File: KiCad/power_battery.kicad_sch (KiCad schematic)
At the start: 47 parts, among them IC1 BQ26221PW, J4 Conn_01x03_BATT, Q2 AO3400A, Q3 AO3400A, U2 DW01A, U3 TXB0101DBV, U4 BQ51050BRHL, U5 PAM2306AYPKE

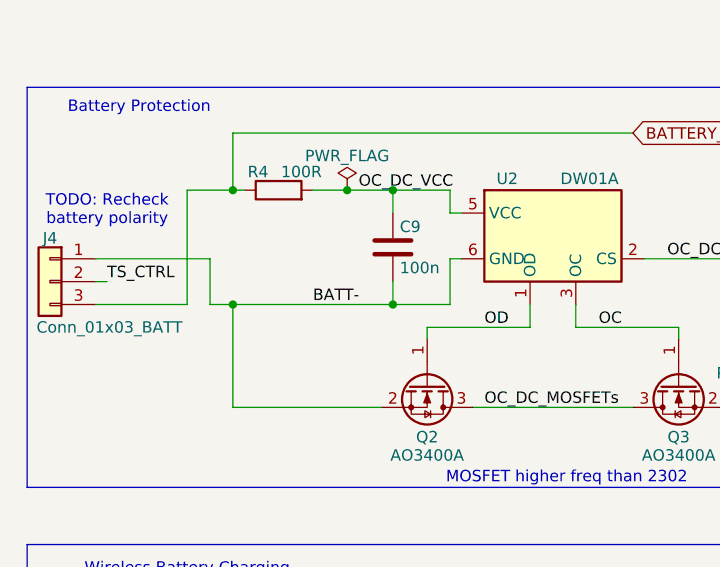
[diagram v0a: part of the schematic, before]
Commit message: Add Power Flag on GND
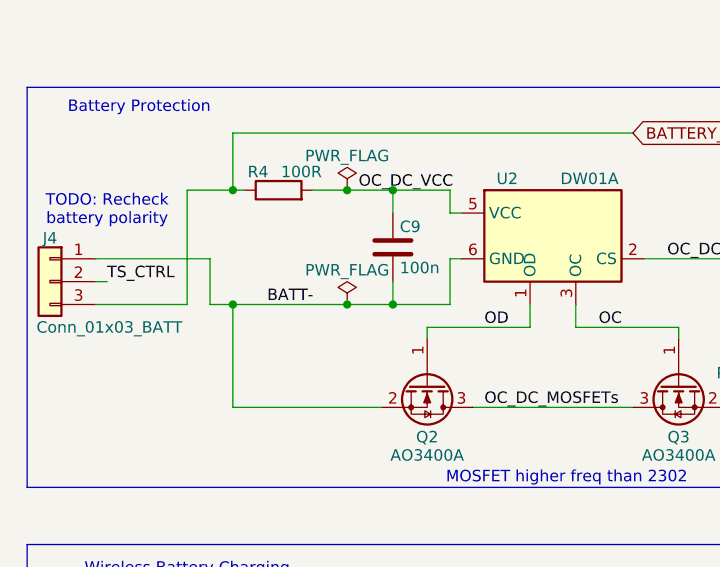
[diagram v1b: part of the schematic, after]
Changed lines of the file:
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@@
 	)
 	(junction
+		(at 54.61 52.07)
+		(diameter 0)
+		(color 0 0 0 0)
+	)
+	(junction
 		(at 41.91 52.07)
 		(diameter 0)
@@
 	(wire
 		(pts
-			(xy 41.91 52.07) (xy 59.69 52.07)
+			(xy 41.91 52.07) (xy 54.61 52.07)
 		)
 		(stroke
@@
 	(wire
 		(pts
+			(xy 54.61 52.07) (xy 59.69 52.07)
+		)
+		(stroke
+			(width 0)
+			(type default)
+		)
+	)
+	(wire
+		(pts
 			(xy 104.14 166.37) (xy 104.14 168.91)
 		)
@@
 	)
 	(label "BATT-"
-		(at 50.8 52.07 0)
+		(at 45.72 52.07 0)
 		(effects
 			(font
@@
 					(unit 1)
 				)
+			)
+		)
+	)
+	(symbol
+		(lib_id "power:PWR_FLAG")
+		(at 54.61 52.07 0)
+		(unit 1)
+		(exclude_from_sim no)
+		(in_bom yes)
+		(on_board yes)
+		(dnp no)
+		(property "Reference" "#FLG06"
+			(at 54.61 50.165 0)
+			(effects
+				(font
+					(size 1.27 1.27)
+				)
+				(hide yes)
+			)
+		)
+		(property "Value" "PWR_FLAG"
+			(at 54.61 48.26 0)
+			(effects
+				(font
+					(size 1.27 1.27)
+				)
+			)
+		)
+		(property "Footprint" ""
+			(at 54.61 52.07 0)
+			(effects
+				(font
+					(size 1.27 1.27)
+				)
+				(hide yes)
+			)
+		)
+		(property "Datasheet" "~"
+			(at 54.61 52.07 0)
+			(effects
+				(font
+					(size 1.27 1.27)
+				)
+				(hide yes)
+			)
+		)
+		(property "Description" "Special symbol for telling ERC where power comes from"
+			(at 54.61 52.07 0)
+			(effects
+				(font
+					(size 1.27 1.27)
+				)
+				(hide yes)
+			)
+		)
+		(pin "1"
+		)
+		(instances
+			(project "STDC"
+				(path "/643c756f-a801-466b-9148-7370ee6a5e00/6fbfac7b-b6a0-440e-84eb-56b1f74b7943"
+					(reference "#FLG06")
+					(unit 1)
+				)

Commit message: Create Revision 0.0.1
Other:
- company: (none) -> ETH Zurich: Center for Project Based Learning
- title: (none) -> STDC: Power & Battery
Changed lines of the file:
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@@
 	(generator_version "9.0")
 	(paper "A4")
+	(title_block
+		(title "STDC: Power & Battery")
+		(date "2026-03-05")
+		(rev "0.0.1")
+		(company "ETH Zurich: Center for Project Based Learning")
+	)
 	(rectangle
 		(start 19.05 78.74)

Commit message: Add TODO to discuss tomorrow
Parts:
- R11: value 1k -> 680R
- R15: value 200R -> 220R
- R16: value 2.4k -> 2k2
- R4: value 100R -> 150R
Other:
- note added: "R_{FOD} = 220R => R_ILIM=150R => 370R close to 375R target I_{BULk}=K_{ILIM} / R_{ILIM} = 300 / 370 = 811mA = 0.8A"
- note added: "R_{TERM}: Original 2k4, with 2k2: 9.17% Term Current with 2k4: 10% Term Current"
- note added: "TODO: Where should this (FGND) tie to?"
- note removed: "I_{BULk}=800mA R_{ILIM}=393R/(0.8A)=393R R_{FOD} = 220R => R_ILIM=173R"
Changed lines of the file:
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@@
 		)
 	)
-	(text "I_{BULk}=800mA\nR_{ILIM}=393R/(0.8A)=393R\nR_{FOD} = 220R => R_ILIM=173R"
+	(text "R_{FOD} = 220R => R_ILIM=150R => 370R\nclose to 375R target\nI_{BULk}=K_{ILIM} / R_{ILIM} = 300 / 370 = 811mA = 0.8A"
 		(exclude_from_sim no)
-		(at 159.004 145.034 0)
+		(at 142.494 136.144 0)
 		(effects
 			(font
@@
 		)
 	)
+	(text "TODO: Where should this \n(FGND) tie to?"
+		(exclude_from_sim no)
+		(at 266.7 66.548 0)
+		(effects
+			(font
+				(size 1.27 1.27)
+			)
+		)
+	)
 	(text "Wireless Charging RX Coil"
 		(exclude_from_sim no)
@@
 		)
 	)
+	(text "R_{TERM}: Original 2k4, \nwith 2k2: 9.17% Term Current\nwith 2k4: 10% Term Current"
+		(exclude_from_sim no)
+		(at 192.278 144.526 0)
+		(effects
+			(font
+				(size 1.27 1.27)
+			)
+		)
+	)
 	(text "TODO: Recheck \nbattery polarity"
 		(exclude_from_sim no)
@@
 		(dnp no)
 		(property "Reference" "R11"
-			(at 183.642 92.456 90)
+			(at 182.372 92.456 90)
 			(effects
 				(font
@@
 			)
 		)
-		(property "Value" "1k"
-			(at 187.96 92.456 90)
+		(property "Value" "680R"
+			(at 188.468 92.456 90)
 			(effects
 				(font
@@
 			)
 		)
-		(property "Value" "100R"
+		(property "Value" "150R"
 			(at 49.53 37.338 90)
 			(effects
@@
 			)
 		)
-		(property "Value" "200R"
+		(property "Value" "220R"
 			(at 170.18 137.16 0)
 			(effects
@@
 			)
 		)
-		(property "Value" "2.4k"
+		(property "Value" "2k2"
 			(at 179.07 137.16 0)
 			(effects

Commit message: Added some TODOs, fixed some TODOs
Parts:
- added C15: 100n, symbol Device:C
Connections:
- net BAT_STAT_C_COUNT is gone; now on net GND: R10.2, R8.2
- net +1V8: now also C15.1
- net +3.3V: no longer R17.2
- net BATT-: now also C10.2, C11.2, C12.2, C13.2, IC1.3 (VSS), R10.1, R6.2, R7.2, U3.2 (GND), C15.2
- net GND: no longer C10.2, C11.2, C12.2, C13.2, IC1.3 (VSS), R10.1, R6.2, R7.2, U3.2 (GND)
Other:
- note added: "TODO: Saturation Current at Peak Current * DCDc With Display ON?"
- note removed: "TODO: Where should this (FGND) tie to?"
- moved on the sheet: C10, C11, C12, C13, IC1, R10, R6, R7, R9, U3

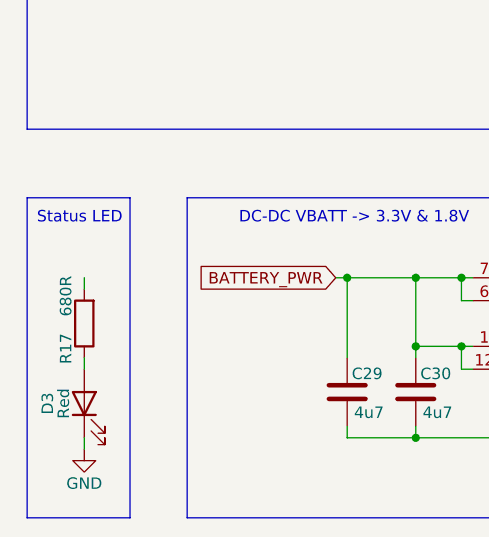
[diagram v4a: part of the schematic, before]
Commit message: Fix JTAG connector
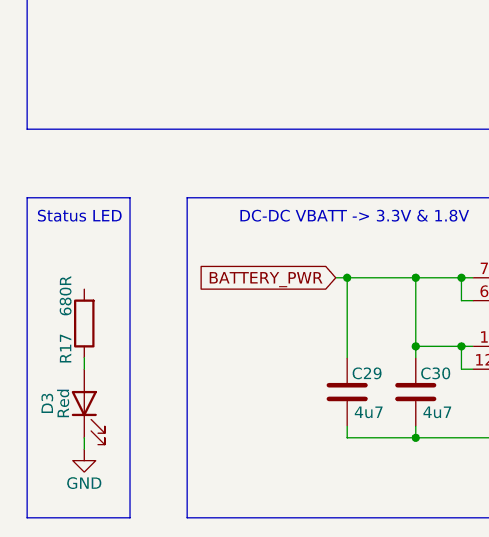
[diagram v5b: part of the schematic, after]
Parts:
- C15: footprint (none) -> Capacitor_SMD:C_0402_1005Metric
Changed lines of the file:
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@@
-	(wire
-		(pts
-			(xy 25.4 166.37) (xy 25.4 167.64)
-		)
-		(stroke
-			(width 0)
-			(type default)
-		)
-	)
 	(wire
 		(pts
@@
 			)
 		)
-		(property "Footprint" ""
+		(property "Footprint" "Capacitor_SMD:C_0402_1005Metric"
 			(at 141.9352 62.23 0)
 			(effects

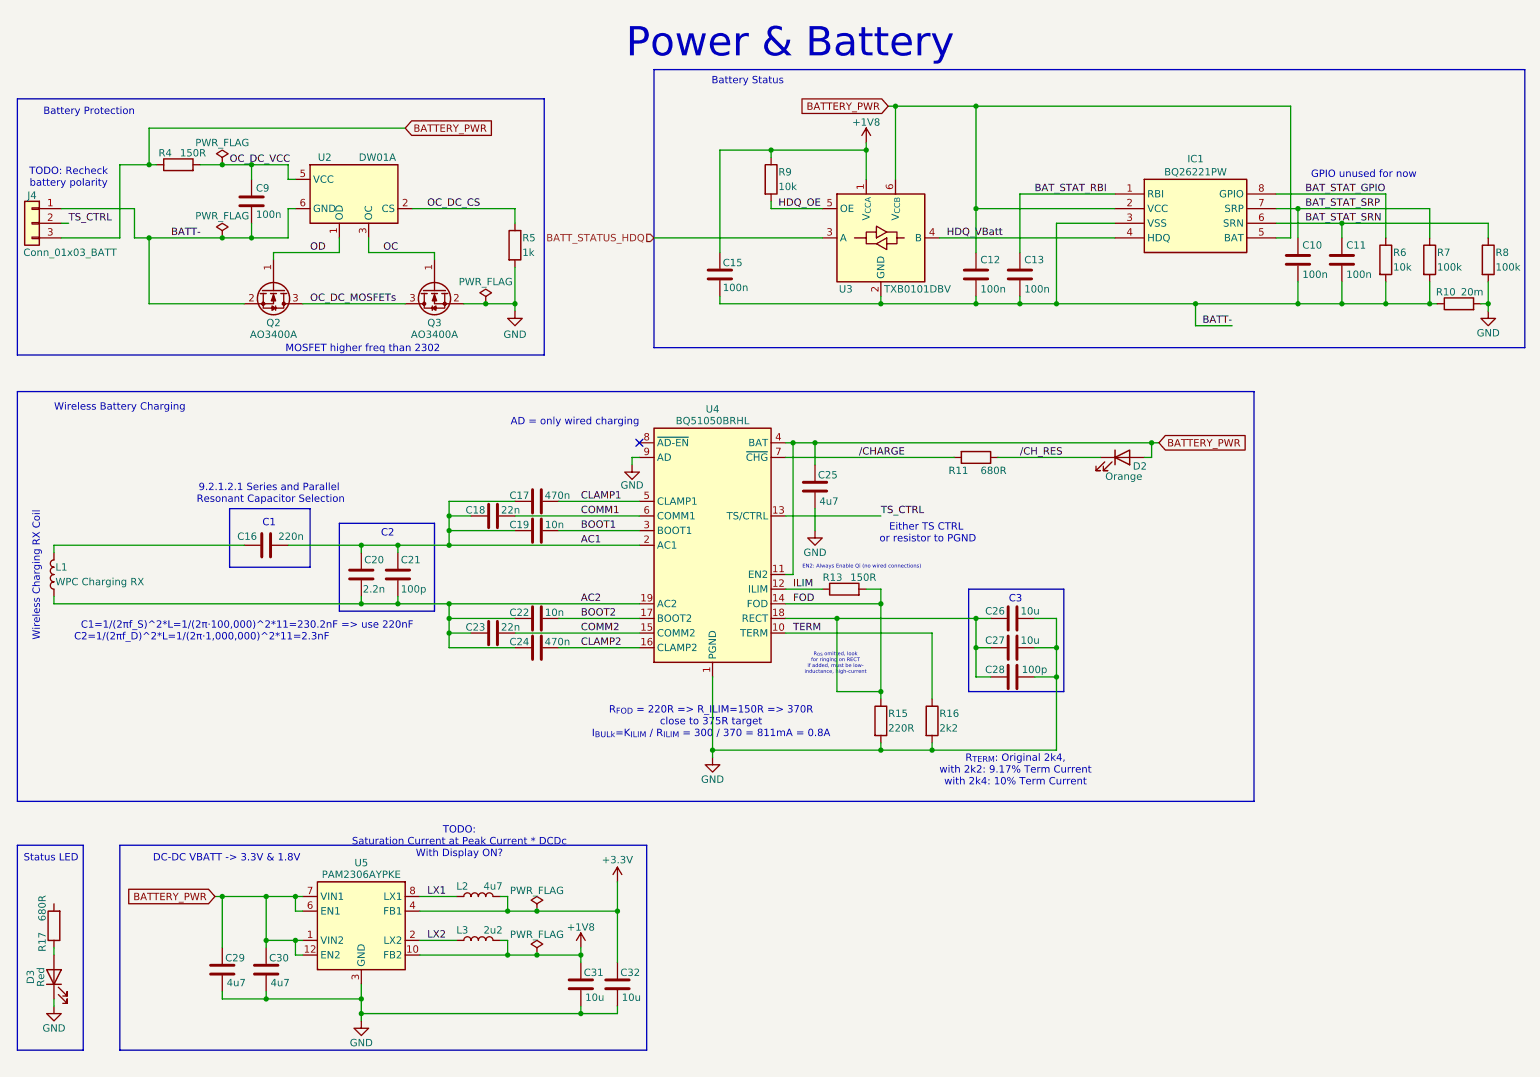
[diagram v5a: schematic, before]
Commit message: Testing connectors, SPI2 pinout, reannotate
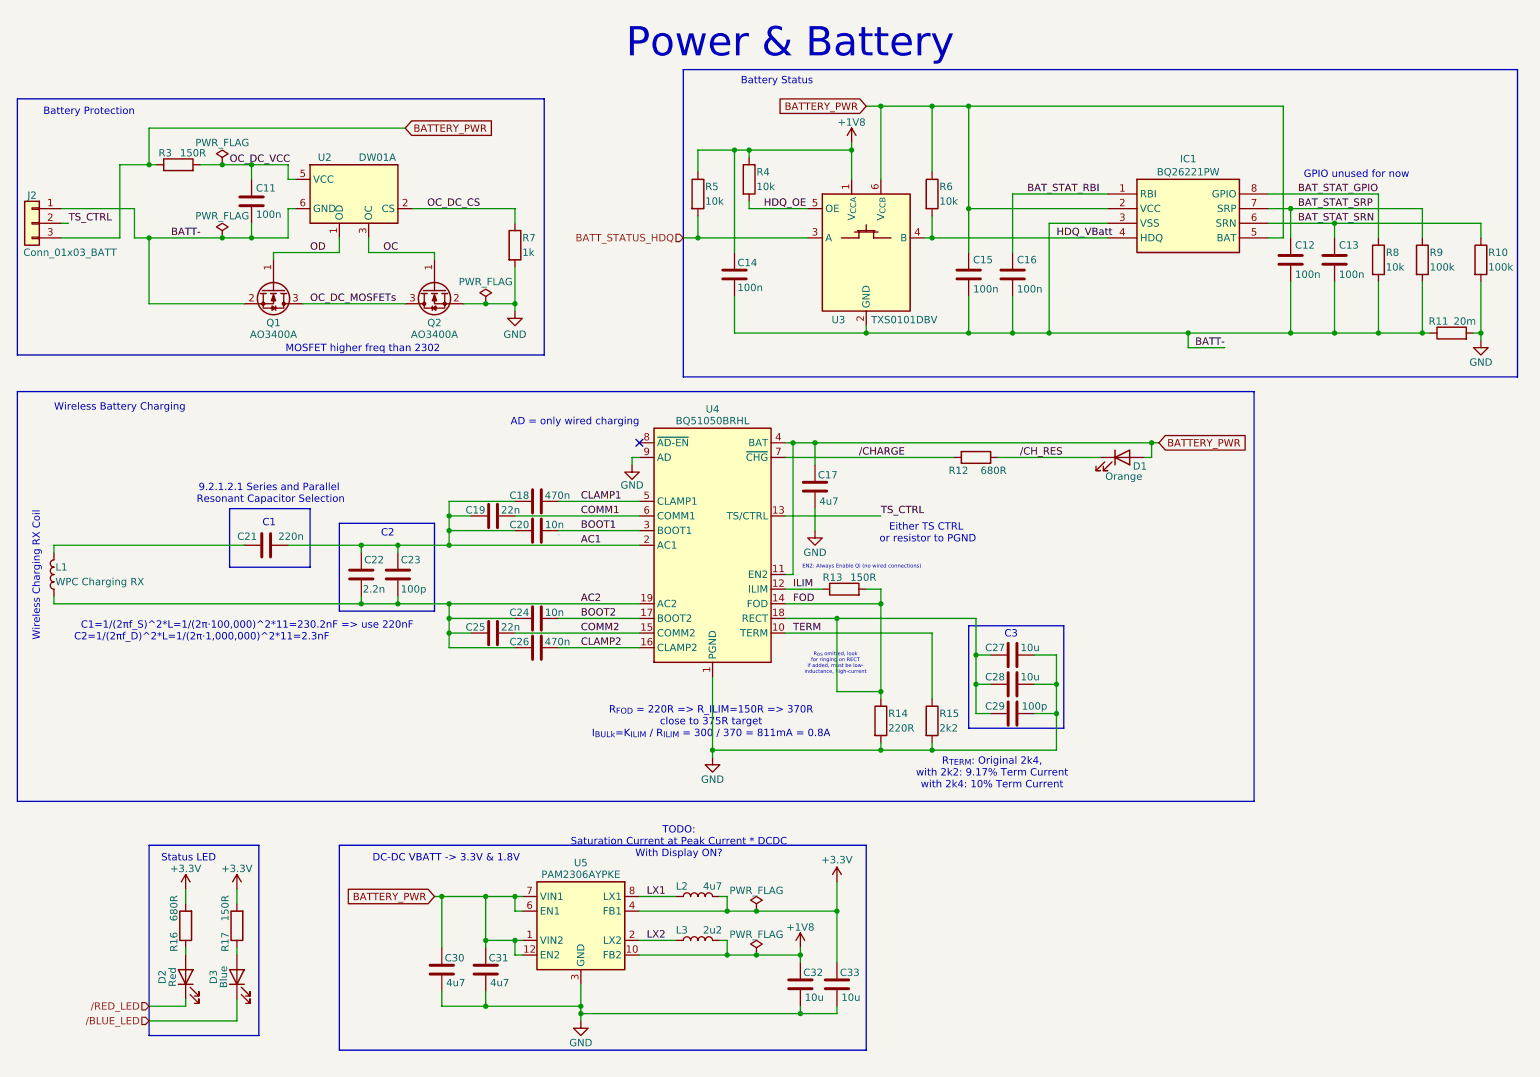
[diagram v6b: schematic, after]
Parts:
- removed U3: TXB0101DBV, Package_TO_SOT_SMD:SOT-23-6, symbol Logic_LevelTranslator:TXB0101DBV
- added D3: Blue, LED_SMD:LED_0603_1608Metric, symbol Device:LED
- added R17: 150R, Resistor_SMD:R_0402_1005Metric, symbol Device:R
- added R5, R6: 10k, Resistor_SMD:R_0402_1005Metric, symbol Device:R
- added U3: TXS0101DBV, Package_TO_SOT_SMD:SOT-23-6, symbol Logic_LevelTranslator:TXS0101DBV
- renumbered C9 to C11, C10 to C12, C11 to C13, C15 to C14, C12 to C15, C13 to C16, C25 to C17, C17 to C18, C18 to C19, C19 to C20, C16 to C21, C20 to C22, C21 to C23, C22 to C24, C23 to C25, C24 to C26, C26 to C27, C27 to C28, C28 to C29, C29 to C30, C30 to C31, C31 to C32, C32 to C33, D2 to D1, D3 to D2, J4 to J2, Q2 to Q1, Q3 to Q2, R8 to R10, R10 to R11, R11 to R12, R15 to R14, R16 to R15, R17 to R16, R4 to R3, R9 to R4, R5 to R7, R6 to R8, R7 to R9
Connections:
- net +1V8: now also R5.1, U3.1 (V_{CCA})
- net +3.3V: now also R16.2, R17.2
- net BATT-: now also U3.2 (GND)
- net BATTERY_PWR: now also R6.1, U3.6 (V_{CCB})
- net BATT_STATUS_HDQ: now also R5.2, U3.3 (A)
- net GND: no longer D2.1 (K)
- net HDQ_OE: now also U3.5 (OE)
- net HDQ_VBatt: now also R6.2, U3.4 (B)
- new net: D3.2 (A), R17.1
- new net /BLUE_LED: D3.1 (K)
- new net /RED_LED: D2.1 (K)
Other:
- note added: "TODO: Saturation Current at Peak Current * DCDC With Display ON?"
- note removed: "TODO: Recheck battery polarity"
- note removed: "TODO: Saturation Current at Peak Current * DCDc With Display ON?"
- moved on the sheet: C12, C13, C14, C15, C16, C27, C28, C29, C30, C31, C32, C33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

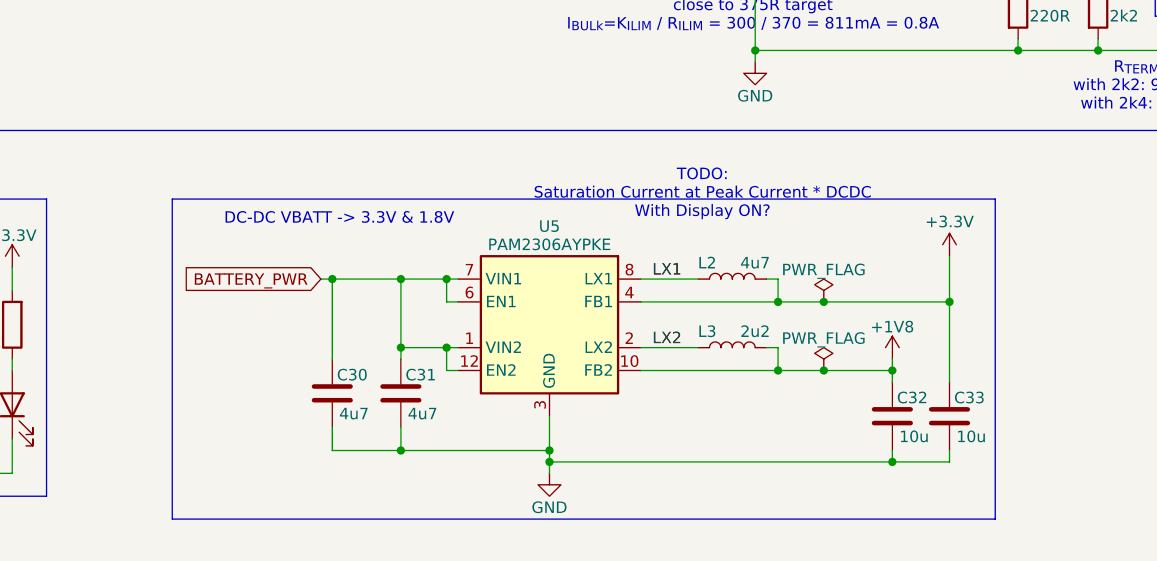
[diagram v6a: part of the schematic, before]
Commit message: Calculate saturation current for coils and add comments
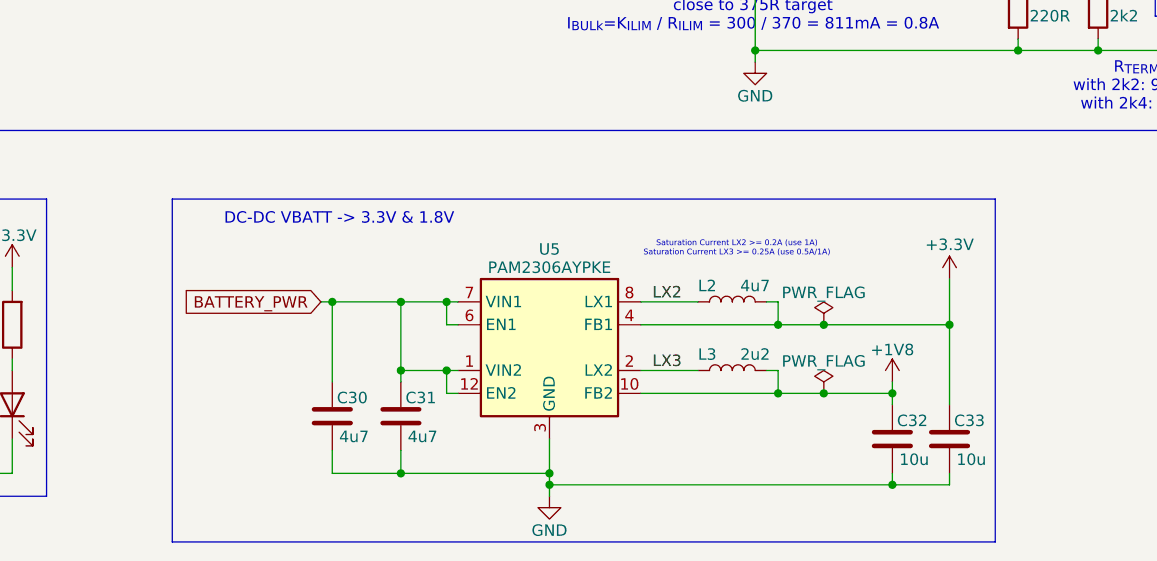
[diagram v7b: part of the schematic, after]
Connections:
- net LX1 is gone; now on net LX2: L2.1, U5.8 (LX1)
- net LX2: no longer L3.1, U5.2 (LX2)
- new net LX3: L3.1, U5.2 (LX2)
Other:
- note added: "Saturation Current LX2 >= 0.2A (use 1A) Saturation Current LX3 >= 0.25A (use 0.5A/1A)"
- note removed: "TODO: Saturation Current at Peak Current * DCDC With Display ON?"
- moved on the sheet: C30, C31, C32, C33, L2, L3, U5

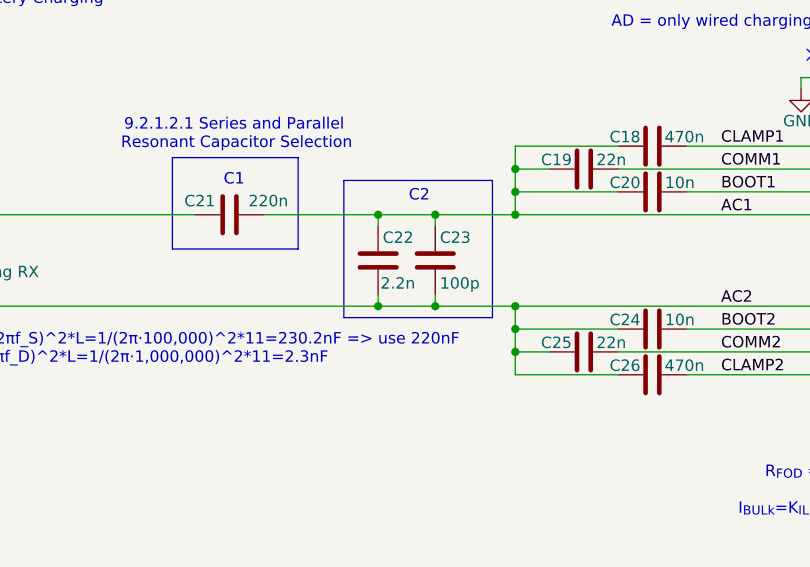
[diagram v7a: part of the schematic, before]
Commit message: Fix display Rs to fix 17V reference and consolidate BOM
And add more info to R_{IREF}
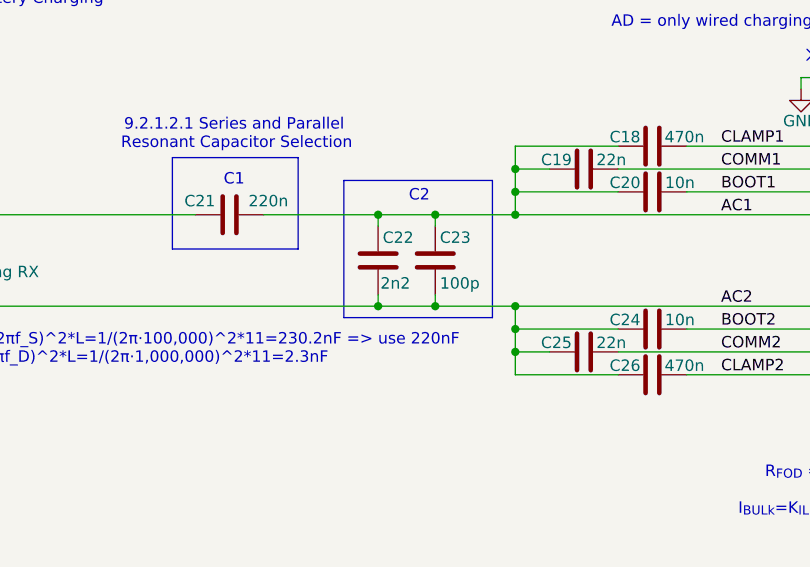
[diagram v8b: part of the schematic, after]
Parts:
- C22: value 2.2n -> 2n2
- L1: now left out of the parts list
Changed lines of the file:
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@@
 		(unit 1)
 		(exclude_from_sim no)
-		(in_bom yes)
+		(in_bom no)
 		(on_board yes)
 		(dnp no)
@@
 			)
 		)
-		(property "Value" "2.2n"
+		(property "Value" "2n2"
 			(at 78.994 113.03 0)
 			(effects
